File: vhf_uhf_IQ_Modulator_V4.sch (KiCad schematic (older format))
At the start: 52 parts, among them J1 CONN_01X03, J2 TEST_1P, J3 Audio-Jack-3, J4 CONN_01X04, J5 SMA Edge FM, Q1 BC817-40, Q2 BC817-40, Q3 BC817-40, U2 MMZ09332BT1, U4 Orange Pi zero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

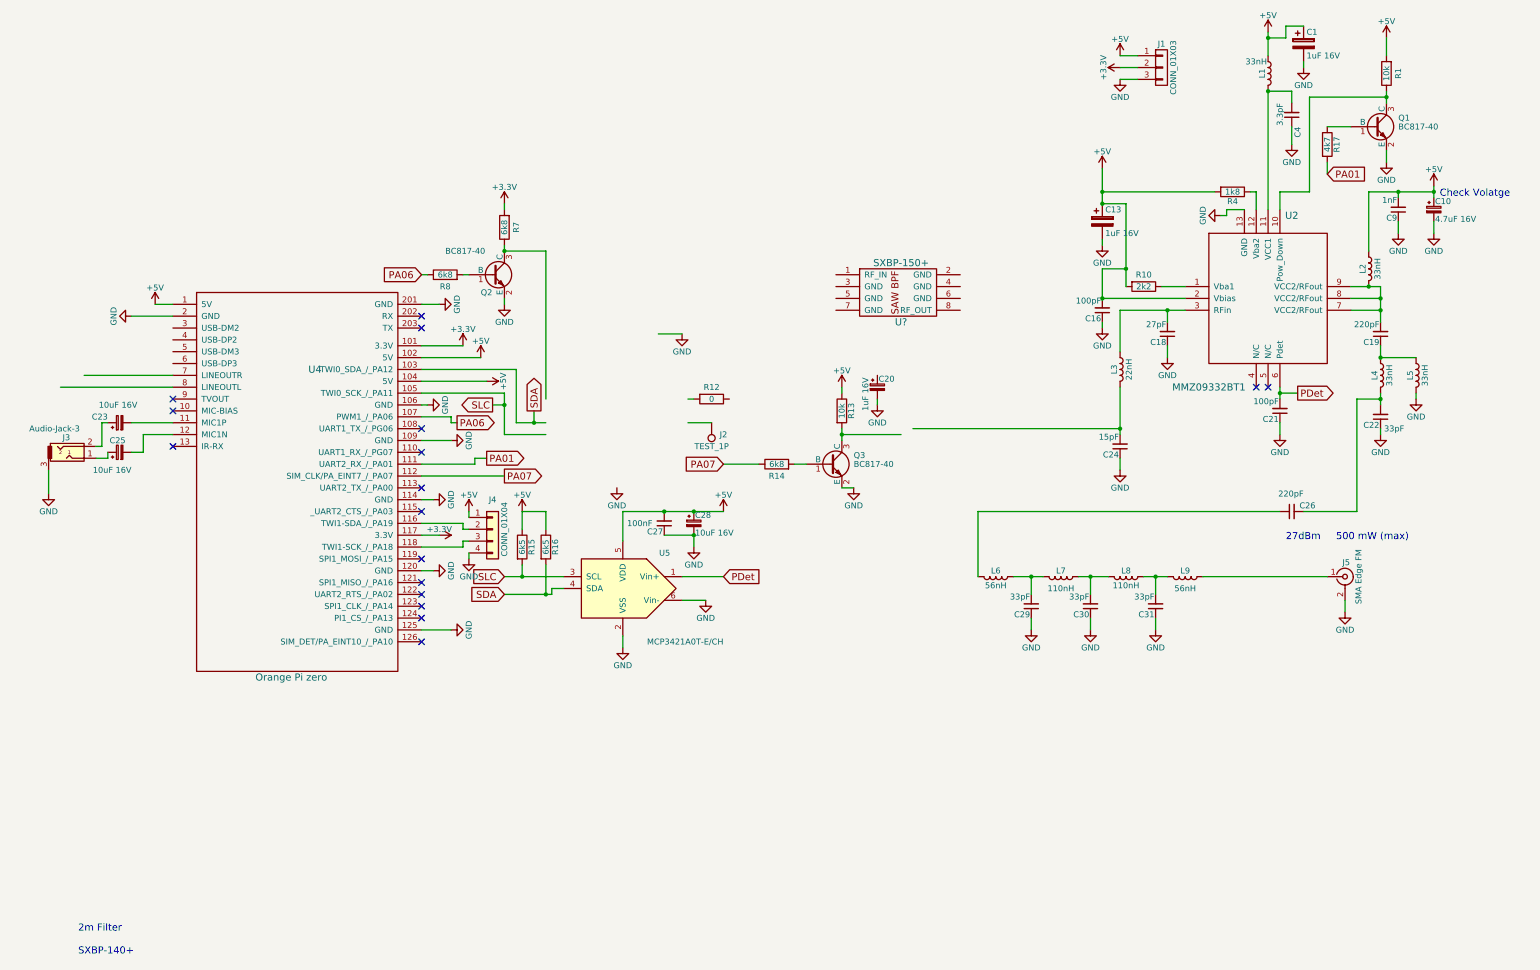
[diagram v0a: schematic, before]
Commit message: pcb placement
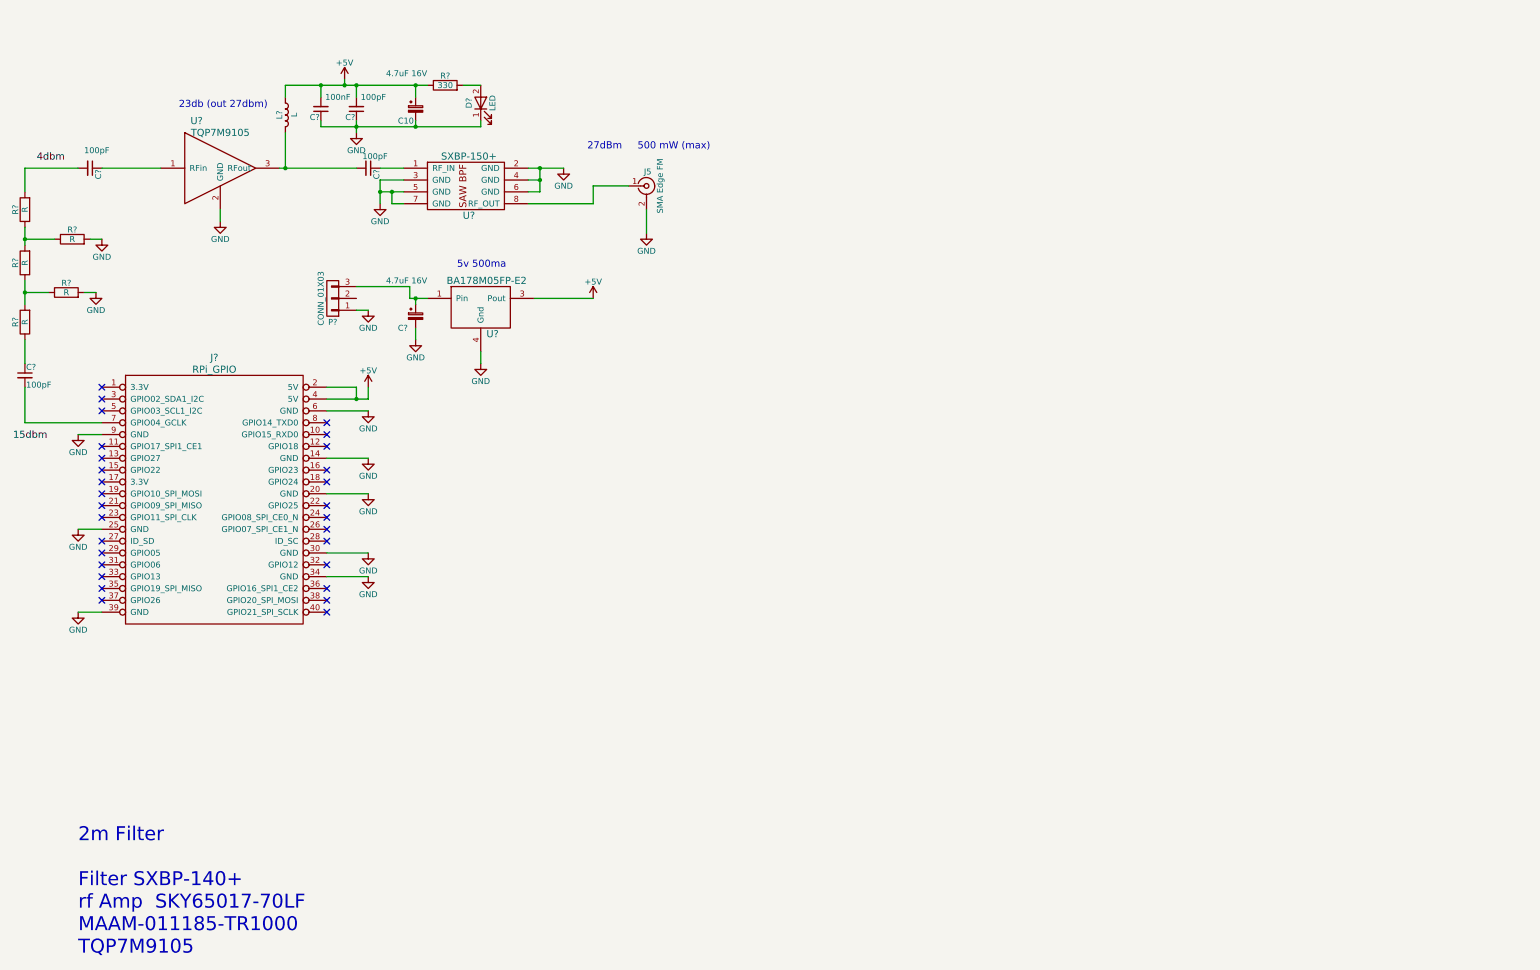
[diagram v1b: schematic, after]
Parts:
- removed C1, C13: 1uF 16V, Capacitors_Tantalum_SMD:CP_Tantalum_Case-R_EIA-2012-12_Reflow, symbol CP
- removed C16, C21: 100pF, Capacitors_SMD:C_0805_HandSoldering, symbol C_Small
- removed C18: 27pF, Capacitors_SMD:C_0805_HandSoldering, symbol C_Small
- removed C19, C26: 220pF, Capacitors_SMD:C_0805_HandSoldering, symbol C_Small
- removed C20: 1uF 16V, Capacitors_Tantalum_SMD:CP_Tantalum_Case-R_EIA-2012-12_Reflow, symbol CP_Small
- removed C22, C29, C30, C31: 33pF, Capacitors_SMD:C_0805_HandSoldering, symbol C_Small
- removed C23, C25, C28: 10uF 16V, Capacitors_SMD:C_0805_HandSoldering, symbol CP_Small
- removed C24: 15pF, Capacitors_SMD:C_0805_HandSoldering, symbol C_Small
- removed C27: 100nF, Capacitors_SMD:C_0805_HandSoldering, symbol C_Small
- removed C4: 3.3pF, Capacitors_SMD:C_0805_HandSoldering, symbol C_Small
- removed C9: 1nF, Capacitors_SMD:C_0805_HandSoldering, symbol C_Small
- removed J1: CONN_01X03, Pin_Headers:Pin_Header_Straight_1x03_Pitch2.54mm, symbol CONN_01X03
- removed J2: TEST_1P, Pin_Headers:Pin_Header_Straight_1x01_Pitch2.54mm, symbol TEST_1P
- removed J3: Audio-Jack-3, Pin_Headers:Pin_Header_Straight_1x03_Pitch2.54mm, symbol Audio-Jack-3
- removed J4: CONN_01X04, Pin_Headers:Pin_Header_Straight_1x04_Pitch2.54mm, symbol Conn_01x04
- removed L1, L5: 33nH, Capacitors_SMD:C_0805_HandSoldering, symbol L
- removed L2, L4: 33nH, Inductors_SMD:L_0805_HandSoldering, symbol L
- removed L3: 22nH, Capacitors_SMD:C_0805_HandSoldering, symbol L
- removed L6, L9: 56nH, Inductors_SMD:L_0805_HandSoldering, symbol L
- removed L7, L8: 110nH, Inductors_SMD:L_0805_HandSoldering, symbol L
- removed Q1, Q2, Q3: BC817-40, TO_SOT_Packages_SMD:SOT-23, symbol BC817-40
- removed R1, R13: 10k, Resistors_SMD:R_0805_HandSoldering, symbol R
- removed R10: 2k2, Resistors_SMD:R_0805_HandSoldering, symbol R
- removed R12: 0, Resistors_SMD:R_0805_HandSoldering, symbol R
- removed R14, R7, R8: 6k8, Resistors_SMD:R_0805_HandSoldering, symbol R
- removed R15, R16: 6k5, Resistors_SMD:R_0805_HandSoldering, symbol R
- removed R17: 4k7, Resistors_SMD:R_0805_HandSoldering, symbol R
- removed R4: 1k8, Resistors_SMD:R_0805_HandSoldering, symbol R
- removed U2: MMZ09332BT1, QFN-12-1EP_3x3mm:QFN-12-1EP_3x3mm_P0.5mm_EP1.65x1.65mm, symbol MMZ09332BT1
- removed U4: Orange Pi zero, orangepi-zero:orangepi-zero, symbol orange_pi_zero
- removed U5: MCP3421A0T-E/CH, TO_SOT_Packages_SMD:SOT-23-6_Handsoldering, symbol MCP3421A0T-E/CH-RESCUE-vhf_uhf_IQ_Modulator
- removed U?: SXBP-150+, symbol SXBP-150+
- added C? (x4): 100pF, symbol C_Small
- added C?: 100nF, symbol C_Small
- added C?: 4.7uF 16V, Capacitors_SMD:C_0805_HandSoldering, symbol CP_Small
- added D?: LED, symbol LED
- added J?: RPi_GPIO, symbol RPi_GPIO
- added L?: L, symbol L
- added P?: CONN_01X03, symbol CONN_01X03
- added R? (x5): R, symbol R
- added R?: 330, symbol R
- added U?: SXBP-150+, symbol SXBP-150+
- added U?: TQP7M9105, symbol TQP7M9105
- added U?: BA178M05FP-E2, symbol BA178M05FP-E2
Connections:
- net labels added: 15dbm, 4dbm
- net labels removed: +3.3V, PA01, PA06, PA07, PDet, SDA, SLC
- wire segments 157 -> 61
- no-connect marks 17 -> 29
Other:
- note added: "23db (out 27dbm)"
- note added: "2m Filter\n\nFilter SXBP-140+\nrf Amp SKY65017-70LF\nMAAM-011185-TR1000 \nTQP7M9105"
- note added: "5v 500ma"
- note removed: "2m Filter\n\nSXBP-140+"
- note removed: "Check Volatge"
- moved on the sheet: C10, J5
